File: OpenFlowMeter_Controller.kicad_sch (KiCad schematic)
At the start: 41 parts, among them J3 Conn_01x06, J5 Conn_01x03, J6 Conn_02x04_Odd_Even, J7 Conn_02x03_Odd_Even, U2 STM32F103C8Tx, U5 SN65HVD231, U7 24LC64, Y1 12 MHz

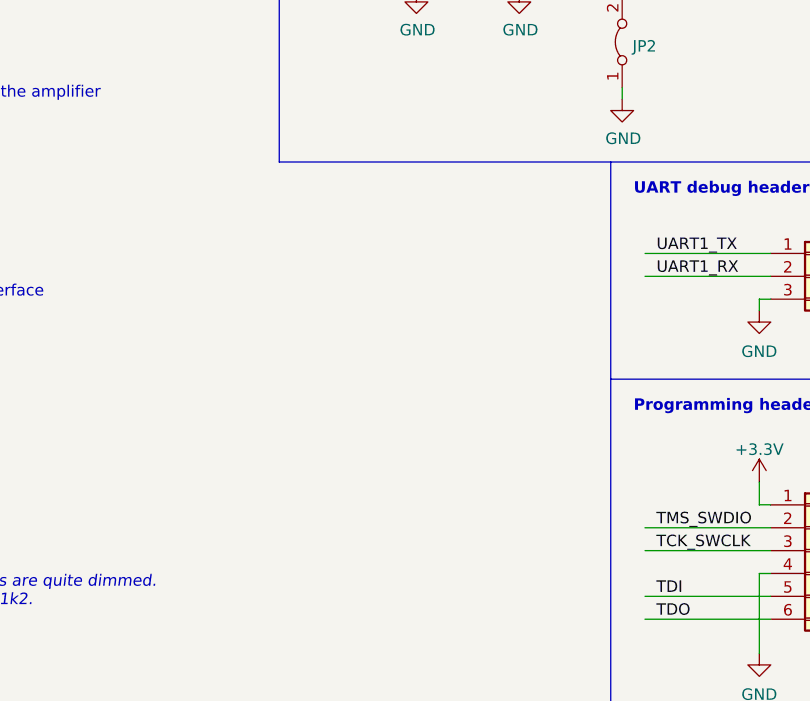
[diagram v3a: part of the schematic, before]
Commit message: added TMP100 as board temperature sensor
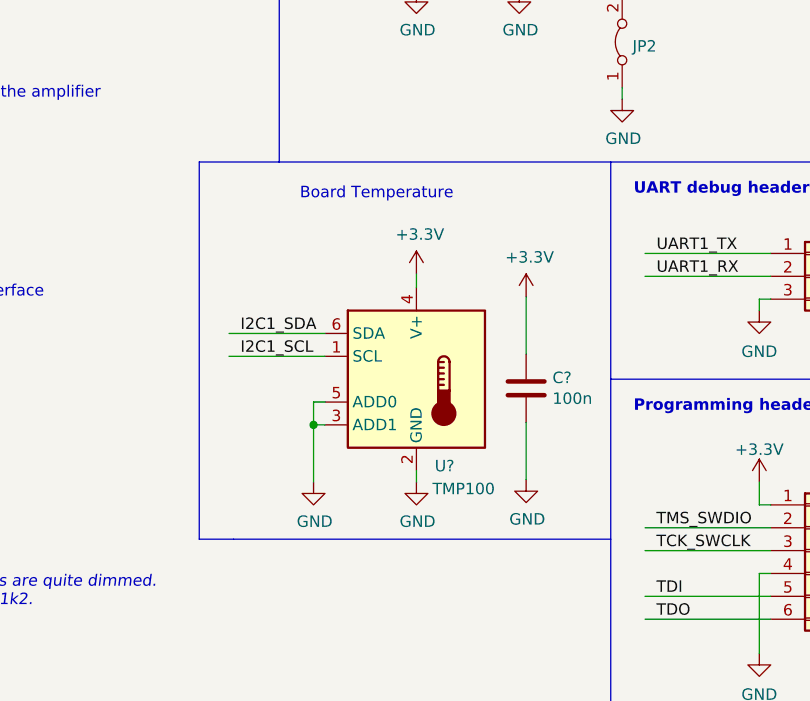
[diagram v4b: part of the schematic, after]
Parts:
- added C?: 100n, Capacitor_SMD:C_0603_1608Metric, symbol Device:C
- added U?: TMP100, Package_TO_SOT_SMD:SOT-23-6, symbol Sensor_Temperature:TMP100
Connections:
- net +3V3: now also C?.1, U?.4 (V+)
- net GND: now also C?.2, U?.2 (GND), U?.3 (ADD1), U?.5 (ADD0)
- net I2C1_SCL: now also U?.1 (SCL)
- net I2C1_SDA: now also U?.6 (SDA)
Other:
- note added: "Board Temperature"
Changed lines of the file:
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@@
   (junction (at 118.11 128.27) (diameter 0) (color 0 0 0 0)
+  )
+  (junction (at 209.55 132.08) (diameter 0) (color 0 0 0 0)
   )
   (junction (at 243.84 77.47) (diameter 0) (color 0 0 0 0)
@@
     (stroke (width 0) (type default) (color 0 0 0 0))
   )
+  (wire (pts (xy 233.172 117.856) (xy 233.172 124.206))
+    (stroke (width 0) (type default) (color 0 0 0 0))
+  )
   (wire (pts (xy 220.98 74.93) (xy 222.25 74.93))
     (stroke (width 0) (type default) (color 0 0 0 0))
@@
     (stroke (width 0) (type default) (color 0 0 0 0))
   )
+  (wire (pts (xy 210.82 132.08) (xy 209.55 132.08))
+    (stroke (width 0) (type default) (color 0 0 0 0))
+  )
   (wire (pts (xy 220.98 74.93) (xy 220.98 72.39))
     (stroke (width 0) (type default) (color 0 0 0 0))
@@
     (stroke (width 0) (type default) (color 0 0 0 0))
   )
+  (wire (pts (xy 200.152 121.92) (xy 210.82 121.92))
+    (stroke (width 0) (type default) (color 0 0 0 0))
+  )
   (wire (pts (xy 208.28 30.48) (xy 222.25 30.48))
     (stroke (width 0) (type default) (color 0 0 0 0))
@@
     (stroke (width 0) (type default) (color 0 0 0 0))
   )
+  (polyline (pts (xy 200.66 144.78) (xy 196.85 144.78))
+    (stroke (width 0) (type default) (color 0 0 0 0))
+  )
   (wire (pts (xy 246.38 151.13) (xy 260.35 151.13))
     (stroke (width 0) (type default) (color 0 0 0 0))
@@
     (stroke (width 0) (type default) (color 0 0 0 0))
   )
+  (wire (pts (xy 220.98 137.16) (xy 220.98 138.43))
+    (stroke (width 0) (type default) (color 0 0 0 0))
+  )
   (wire (pts (xy 109.22 193.04) (xy 109.22 179.07))
     (stroke (width 0) (type default) (color 0 0 0 0))
@@
     (stroke (width 0) (type default) (color 0 0 0 0))
   )
+  (wire (pts (xy 220.98 115.316) (xy 220.98 116.84))
+    (stroke (width 0) (type default) (color 0 0 0 0))
+  )
   (wire (pts (xy 232.41 43.18) (xy 232.41 44.45))
     (stroke (width 0) (type default) (color 0 0 0 0))
@@
     (stroke (width 0) (type default) (color 0 0 0 0))
   )
+  (wire (pts (xy 209.55 129.54) (xy 209.55 132.08))
+    (stroke (width 0) (type default) (color 0 0 0 0))
+  )
   (polyline (pts (xy 101.6 147.32) (xy 158.75 147.32))
     (stroke (width 0) (type default) (color 0 0 0 0))
@@
     (stroke (width 0) (type default) (color 0 0 0 0))
   )
+  (wire (pts (xy 210.82 129.54) (xy 209.55 129.54))
+    (stroke (width 0) (type default) (color 0 0 0 0))
+  )
   (wire (pts (xy 119.38 128.27) (xy 120.65 128.27))
     (stroke (width 0) (type default) (color 0 0 0 0))
@@
     (stroke (width 0) (type default) (color 0 0 0 0))
   )
+  (wire (pts (xy 200.152 124.46) (xy 210.82 124.46))
+    (stroke (width 0) (type default) (color 0 0 0 0))
+  )
   (wire (pts (xy 88.9 104.14) (xy 102.87 104.14))
     (stroke (width 0) (type default) (color 0 0 0 0))
   )
+  (wire (pts (xy 233.172 131.826) (xy 233.172 138.176))
+    (stroke (width 0) (type default) (color 0 0 0 0))
+  )
   (wire (pts (xy 135.89 93.98) (xy 149.86 93.98))
     (stroke (width 0) (type default) (color 0 0 0 0))
@@
     (stroke (width 0) (type default) (color 0 0 0 0))
   )
+  (wire (pts (xy 209.55 132.08) (xy 209.55 138.43))
+    (stroke (width 0) (type default) (color 0 0 0 0))
+  )
   (wire (pts (xy 88.9 114.3) (xy 102.87 114.3))
     (stroke (width 0) (type default) (color 0 0 0 0))
@@
     (stroke (width 0) (type default) (color 0 0 0 0))
   )
+  (polyline (pts (xy 200.66 144.78) (xy 242.57 144.78))
+    (stroke (width 0) (type default) (color 0 0 0 0))
+  )
   (wire (pts (xy 96.52 187.96) (xy 96.52 190.5))
     (stroke (width 0) (type default) (color 0 0 0 0))
@@
     (stroke (width 0) (type default) (color 0 0 0 0))
   )
+  (polyline (pts (xy 196.85 102.87) (xy 205.74 102.87))
+    (stroke (width 0) (type default) (color 0 0 0 0))
+  )
   (wire (pts (xy 88.9 99.06) (xy 102.87 99.06))
     (stroke (width 0) (type default) (color 0 0 0 0))
@@
   )
   (wire (pts (xy 16.51 182.88) (xy 30.48 182.88))
+    (stroke (width 0) (type default) (color 0 0 0 0))
+  )
+  (polyline (pts (xy 196.85 144.78) (xy 196.85 102.87))
     (stroke (width 0) (type default) (color 0 0 0 0))
   )
@@
     (effects (font (size 1.27 1.27) (thickness 0.254) bold) (justify left bottom))
   )
+  (text "Board Temperature" (at 208.026 107.188 0)
+    (effects (font (size 1.27 1.27)) (justify left bottom))
+  )
   (text "I2C extension" (at 13.97 166.37 0)
     (effects (font (size 1.27 1.27) (thickness 0.254) bold) (justify left bottom))
@@
     (effects (font (size 1.27 1.27)) (justify left bottom))
   )
+  (label "I2C1_SDA" (at 201.422 121.92 0)
+    (effects (font (size 1.27 1.27)) (justify left bottom))
+  )
   (label "SPI_SCK" (at 20.32 153.67 0)
     (effects (font (size 1.27 1.27)) (justify left bottom))
@@
   )
   (label "SPI_MOSI" (at 90.17 121.92 0)
+    (effects (font (size 1.27 1.27)) (justify left bottom))
+  )
+  (label "I2C1_SCL" (at 201.422 124.46 0)
     (effects (font (size 1.27 1.27)) (justify left bottom))
   )
@@
     )
     (property "Datasheet" "" (id 3) (at 120.65 46.99 0)
+      (effects (font (size 1.27 1.27)) hide)
+    )
+    (pin "1")
+  )
+  (symbol (lib_id "power:GND") (at 209.55 138.43 0) (unit 1)
+    (in_bom yes) (on_board yes)
+    (property "Reference" "#PWR?" (id 0) (at 209.55 144.78 0)
+      (effects (font (size 1.27 1.27)) hide)
+    )
+    (property "Value" "GND" (id 1) (at 209.677 142.8242 0))
+    (property "Footprint" "" (id 2) (at 209.55 138.43 0)
+      (effects (font (size 1.27 1.27)) hide)
+    )
+    (property "Datasheet" "" (id 3) (at 209.55 138.43 0)
+      (effects (font (size 1.27 1.27)) hide)
+    )
+    (pin "1")
+  )
+  (symbol (lib_id "power:+3.3V") (at 233.172 117.856 0) (unit 1)
+    (in_bom yes) (on_board yes)
+    (property "Reference" "#PWR?" (id 0) (at 233.172 121.666 0)
+      (effects (font (size 1.27 1.27)) hide)
+    )
+    (property "Value" "+3.3V" (id 1) (at 233.553 113.4618 0))
+    (property "Footprint" "" (id 2) (at 233.172 117.856 0)
+      (effects (font (size 1.27 1.27)) hide)
+    )
+    (property "Datasheet" "" (id 3) (at 233.172 117.856 0)
       (effects (font (size 1.27 1.27)) hide)
     )
@@
     )
     (property "Datasheet" "" (id 3) (at 271.78 63.5 0)
+      (effects (font (size 1.27 1.27)) hide)
+    )
+    (pin "1")
+  )
+  (symbol (lib_id "power:+3.3V") (at 220.98 115.316 0) (unit 1)
+    (in_bom yes) (on_board yes)
+    (property "Reference" "#PWR?" (id 0) (at 220.98 119.126 0)
+      (effects (font (size 1.27 1.27)) hide)
+    )
+    (property "Value" "+3.3V" (id 1) (at 221.361 110.9218 0))
+    (property "Footprint" "" (id 2) (at 220.98 115.316 0)
+      (effects (font (size 1.27 1.27)) hide)
+    )
+    (property "Datasheet" "" (id 3) (at 220.98 115.316 0)
       (effects (font (size 1.27 1.27)) hide)
     )
@@
     (pin "1")
   )
+  (symbol (lib_id "power:GND") (at 233.172 138.176 0) (unit 1)
+    (in_bom yes) (on_board yes)
+    (property "Reference" "#PWR?" (id 0) (at 233.172 144.526 0)
+      (effects (font (size 1.27 1.27)) hide)
+    )
+    (property "Value" "GND" (id 1) (at 233.299 142.5702 0))
+    (property "Footprint" "" (id 2) (at 233.172 138.176 0)
+      (effects (font (size 1.27 1.27)) hide)
+    )
+    (property "Datasheet" "" (id 3) (at 233.172 138.176 0)
+      (effects (font (size 1.27 1.27)) hide)
+    )
+    (pin "1")
+  )
+  (symbol (lib_id "Sensor_Temperature:TMP100") (at 220.98 127 0) (unit 1)
+    (in_bom yes) (on_board yes)
+    (property "Reference" "U?" (id 0) (at 223.012 136.652 0)
+      (effects (font (size 1.27 1.27)) (justify left))
+    )
+    (property "Value" "TMP100" (id 1) (at 222.758 139.192 0)
+      (effects (font (size 1.27 1.27)) (justify left))
+    )
+    (property "Footprint" "Package_TO_SOT_SMD:SOT-23-6" (id 2) (at 220.98 135.89 0)
+      (effects (font (size 1.27 1.27)) hide)
+    )
+    (property "Datasheet" "http://www.ti.com/lit/gpn/tmp100" (id 3) (at 219.71 127 0)
+      (effects (font (size 1.27 1.27)) hide)
+    )
+    (pin "1")
+    (pin "2")
+    (pin "3")
+    (pin "4")
+    (pin "5")
+    (pin "6")
+  )
   (symbol (lib_id "power:GND") (at 19.05 45.72 0) (unit 1)
     (in_bom yes) (on_board yes)
@@
     (pin "2")
   )
+  (symbol (lib_id "Device:C") (at 233.172 128.016 0) (unit 1)
+    (in_bom yes) (on_board yes)
+    (property "Reference" "C?" (id 0) (at 236.093 126.8476 0)
+      (effects (font (size 1.27 1.27)) (justify left))
+    )
+    (property "Value" "100n" (id 1) (at 236.093 129.159 0)
+      (effects (font (size 1.27 1.27)) (justify left))
+    )
+    (property "Footprint" "Capacitor_SMD:C_0603_1608Metric" (id 2) (at 234.1372 131.826 0)
+      (effects (font (size 1.27 1.27)) hide)
+    )
+    (property "Datasheet" "~" (id 3) (at 233.172 128.016 0)
+      (effects (font (size 1.27 1.27)) hide)
+    )
+    (pin "1")
+    (pin "2")
+  )
+  (symbol (lib_id "power:GND") (at 220.98 138.43 0) (unit 1)
+    (in_bom yes) (on_board yes)
+    (property "Reference" "#PWR?" (id 0) (at 220.98 144.78 0)
+      (effects (font (size 1.27 1.27)) hide)
+    )
+    (property "Value" "GND" (id 1) (at 221.107 142.8242 0))
+    (property "Footprint" "" (id 2) (at 220.98 138.43 0)
+      (effects (font (size 1.27 1.27)) hide)
+    )
+    (property "Datasheet" "" (id 3) (at 220.98 138.43 0)
+      (effects (font (size 1.27 1.27)) hide)
+    )
+    (pin "1")
+  )
   (symbol (lib_id "Device:R") (at 248.92 77.47 90) (unit 1)

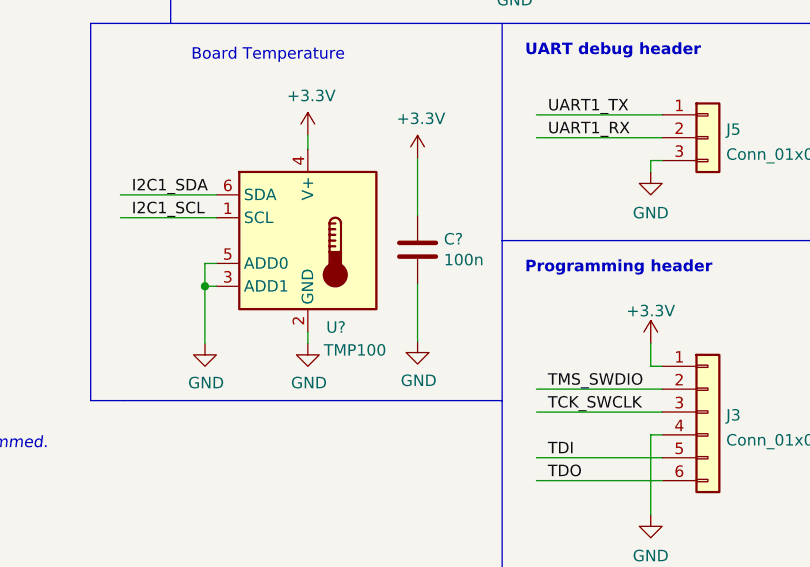
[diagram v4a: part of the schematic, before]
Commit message: fixed DRC for TMP100
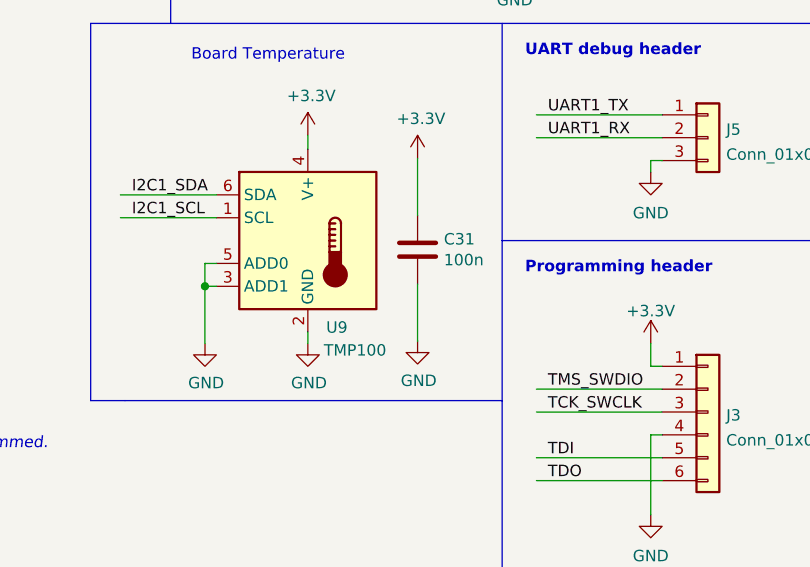
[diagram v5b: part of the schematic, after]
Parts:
- gave numbers to parts that had none: 2
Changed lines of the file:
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@@
   (symbol (lib_id "power:GND") (at 209.55 138.43 0) (unit 1)
     (in_bom yes) (on_board yes)
-    (property "Reference" "#PWR?" (id 0) (at 209.55 144.78 0)
+    (property "Reference" "#PWR075" (id 0) (at 209.55 144.78 0)
       (effects (font (size 1.27 1.27)) hide)
     )
@@
   (symbol (lib_id "power:+3.3V") (at 233.172 117.856 0) (unit 1)
     (in_bom yes) (on_board yes)
-    (property "Reference" "#PWR?" (id 0) (at 233.172 121.666 0)
+    (property "Reference" "#PWR078" (id 0) (at 233.172 121.666 0)
       (effects (font (size 1.27 1.27)) hide)
     )
@@
   (symbol (lib_id "power:+3.3V") (at 220.98 115.316 0) (unit 1)
     (in_bom yes) (on_board yes)
-    (property "Reference" "#PWR?" (id 0) (at 220.98 119.126 0)
+    (property "Reference" "#PWR076" (id 0) (at 220.98 119.126 0)
       (effects (font (size 1.27 1.27)) hide)
     )
@@
   (symbol (lib_id "power:GND") (at 233.172 138.176 0) (unit 1)
     (in_bom yes) (on_board yes)
-    (property "Reference" "#PWR?" (id 0) (at 233.172 144.526 0)
+    (property "Reference" "#PWR079" (id 0) (at 233.172 144.526 0)
       (effects (font (size 1.27 1.27)) hide)
     )
@@
   (symbol (lib_id "Sensor_Temperature:TMP100") (at 220.98 127 0) (unit 1)
     (in_bom yes) (on_board yes)
-    (property "Reference" "U?" (id 0) (at 223.012 136.652 0)
+    (property "Reference" "U9" (id 0) (at 223.012 136.652 0)
       (effects (font (size 1.27 1.27)) (justify left))
     )
@@
   (symbol (lib_id "Device:C") (at 233.172 128.016 0) (unit 1)
     (in_bom yes) (on_board yes)
-    (property "Reference" "C?" (id 0) (at 236.093 126.8476 0)
+    (property "Reference" "C31" (id 0) (at 236.093 126.8476 0)
       (effects (font (size 1.27 1.27)) (justify left))
     )
@@
   (symbol (lib_id "power:GND") (at 220.98 138.43 0) (unit 1)
     (in_bom yes) (on_board yes)
-    (property "Reference" "#PWR?" (id 0) (at 220.98 144.78 0)
-      (effects (font (size 1.27 1.27)) hide)
-    )
+    (property "Reference" "#PWR077" (id 0) (at 220.98 144.78 0)
+      (effects (font (size 1.27 1.27)) hide)
+    )
